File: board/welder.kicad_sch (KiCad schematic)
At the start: 48 parts, among them J1 VIN, J2 Conn_01x10, J3 Barrel_Jack_Switch, J4 USB_B, J5 POS, J6 NEG, J7 GND, Q1 Q_NIGBT_GCE, Q2 Q_NIGBT_GCE, Q3 Q_NIGBT_GCE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

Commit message: Add Cornell Dublier B10 footprint
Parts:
- C20: footprint (none) -> welder:Cornell_Dublier_B10
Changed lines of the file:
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@@
       (effects (font (size 1.27 1.27)) (justify left))
     )
-    (property "Footprint" "" (id 2) (at 379.4252 80.01 0)
+    (property "Footprint" "welder:Cornell_Dublier_B10" (id 2) (at 379.4252 80.01 0)
       (effects (font (size 1.27 1.27)) hide)
     )
@@
     )
     (path "/74e52290-b4a3-4f30-829f-bf68e89657d3"
-      (reference "C20") (unit 1) (value "50 uF") (footprint "")
+      (reference "C20") (unit 1) (value "50 uF") (footprint "welder:Cornell_Dublier_B10")
     )
     (path "/15aa1d89-1ae9-4558-9d8b-606633d6c749"

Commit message: Added big resistor and inductor footprints and updated board
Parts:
- FB1: footprint Inductor_SMD:L_0603_1608Metric -> Inductor_SMD:L_0805_2012Metric
- L1: footprint (none) -> welder:inductor
- R3: footprint (none) -> welder:RES_5931
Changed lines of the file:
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@@
     (property "Reference" "FB1" (id 0) (at 41.8592 118.11 90))
     (property "Value" "Ferrite_Bead" (id 1) (at 41.8592 120.65 90))
-    (property "Footprint" "Inductor_SMD:L_0603_1608Metric" (id 2) (at 41.91 123.952 90)
+    (property "Footprint" "Inductor_SMD:L_0805_2012Metric" (id 2) (at 41.91 123.952 90)
       (effects (font (size 1.27 1.27)) hide)
     )
@@
     (property "Reference" "R3" (id 0) (at 373.38 91.44 90))
     (property "Value" "0.0001" (id 1) (at 373.38 93.98 90))
-    (property "Footprint" "" (id 2) (at 373.38 102.108 90)
+    (property "Footprint" "welder:RES_5931" (id 2) (at 373.38 102.108 90)
       (effects (font (size 1.27 1.27)) hide)
     )
@@
     (property "Reference" "L1" (id 0) (at 373.38 45.72 90))
     (property "Value" "20 uH" (id 1) (at 373.38 48.26 90))
-    (property "Footprint" "" (id 2) (at 373.38 52.07 0)
+    (property "Footprint" "welder:inductor" (id 2) (at 373.38 52.07 0)
       (effects (font (size 1.27 1.27)) hide)
     )
@@
     )
     (path "/4385f506-0231-4a07-94dc-6e37a0993936"
-      (reference "FB1") (unit 1) (value "Ferrite_Bead") (footprint "Inductor_SMD:L_0603_1608Metric")
+      (reference "FB1") (unit 1) (value "Ferrite_Bead") (footprint "Inductor_SMD:L_0805_2012Metric")
     )
     (path "/9a2530d0-2be0-4564-82ea-55a5f02a536a"
@@
     )
     (path "/b52a224f-7f04-4e02-9abf-b091b5cdd9ca"
-      (reference "L1") (unit 1) (value "20 uH") (footprint "")
+      (reference "L1") (unit 1) (value "20 uH") (footprint "welder:inductor")
     )
     (path "/ba154238-685f-413a-8934-e53ce3e1c078"
@@
     )
     (path "/605c0c72-577a-420e-a1f2-9c549bf938f8"
-      (reference "R3") (unit 1) (value "0.0001") (footprint "")
+      (reference "R3") (unit 1) (value "0.0001") (footprint "welder:RES_5931")
     )
     (path "/070672ed-1ab6-4925-9102-8c9f7c67d003"

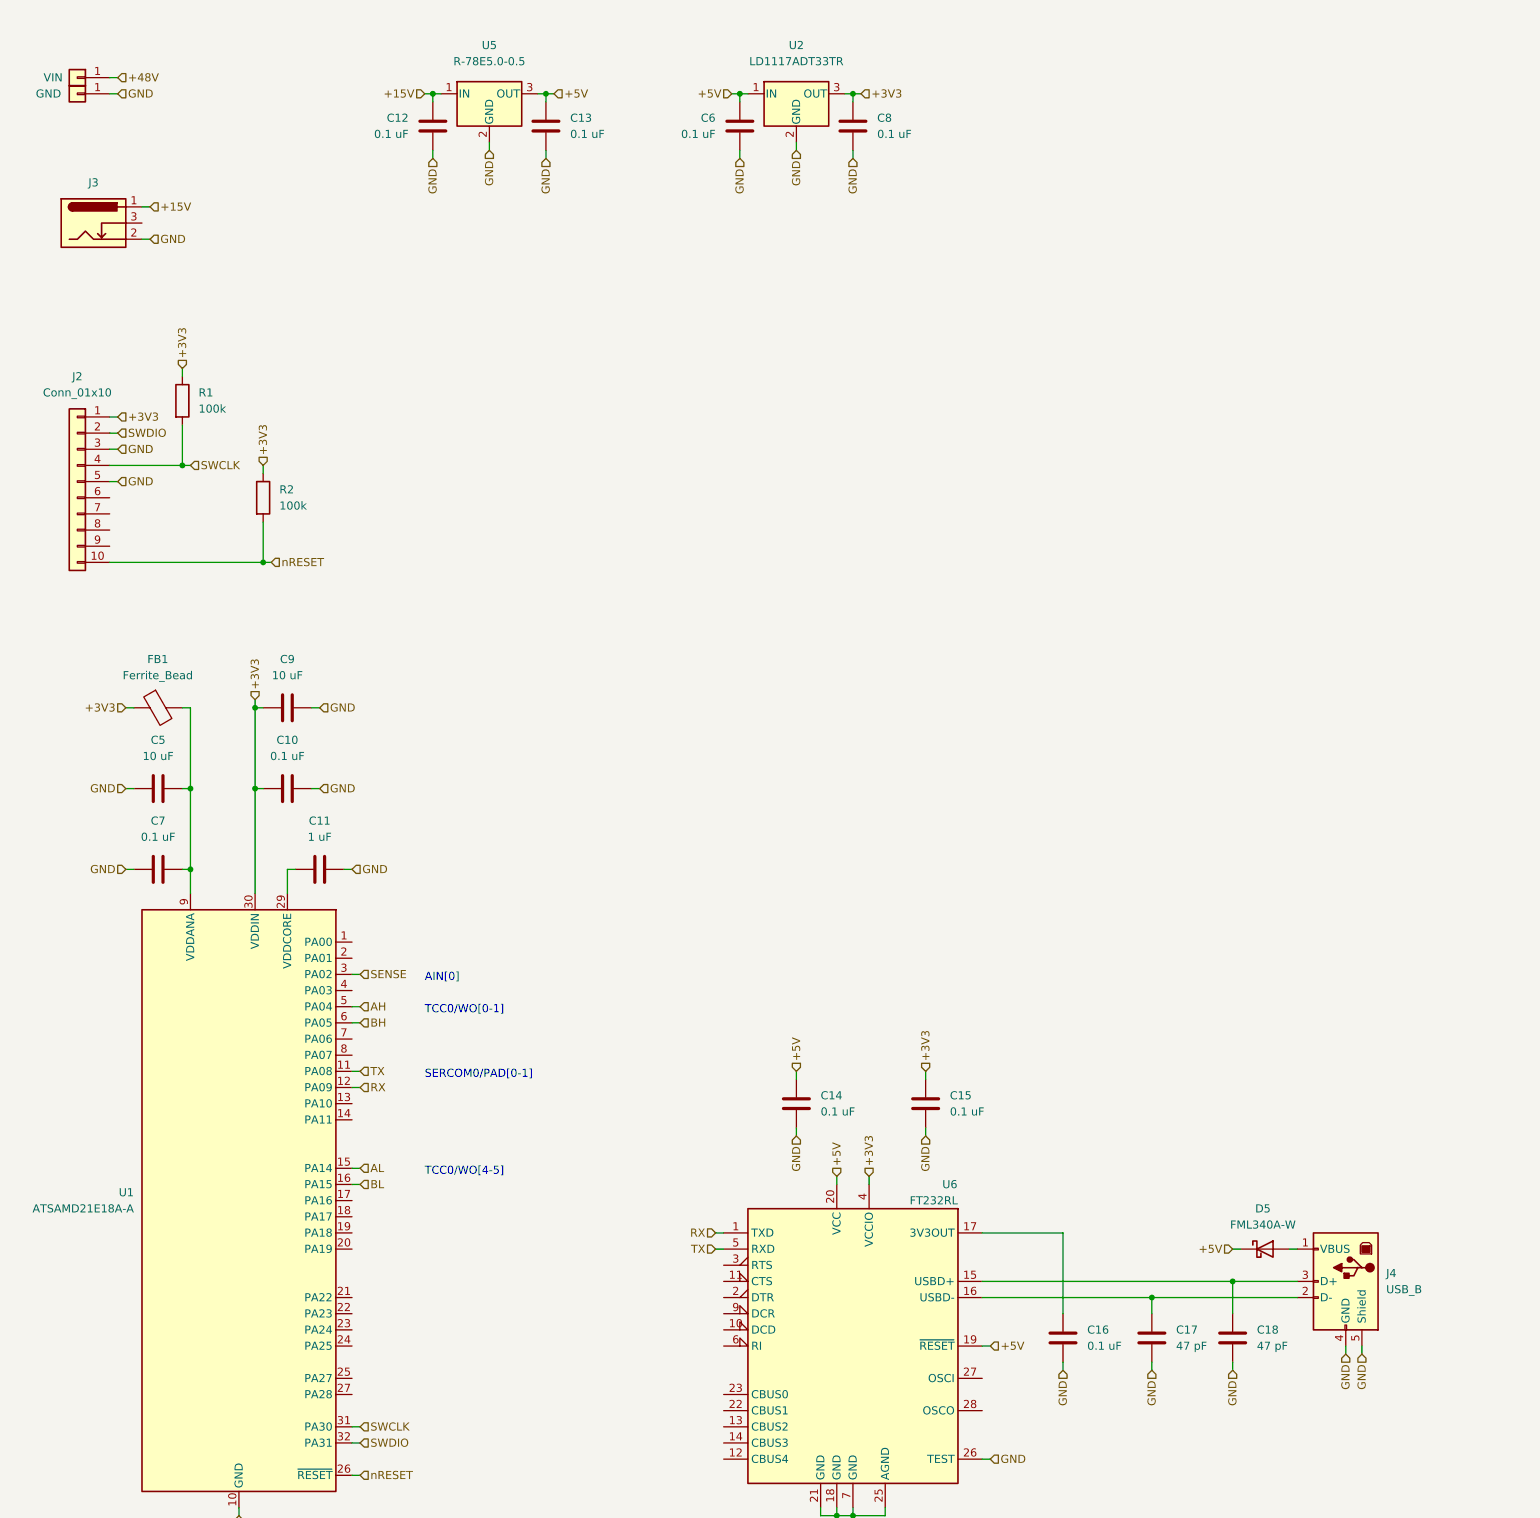
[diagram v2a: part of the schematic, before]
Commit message: added display, fixed up field names, updated board
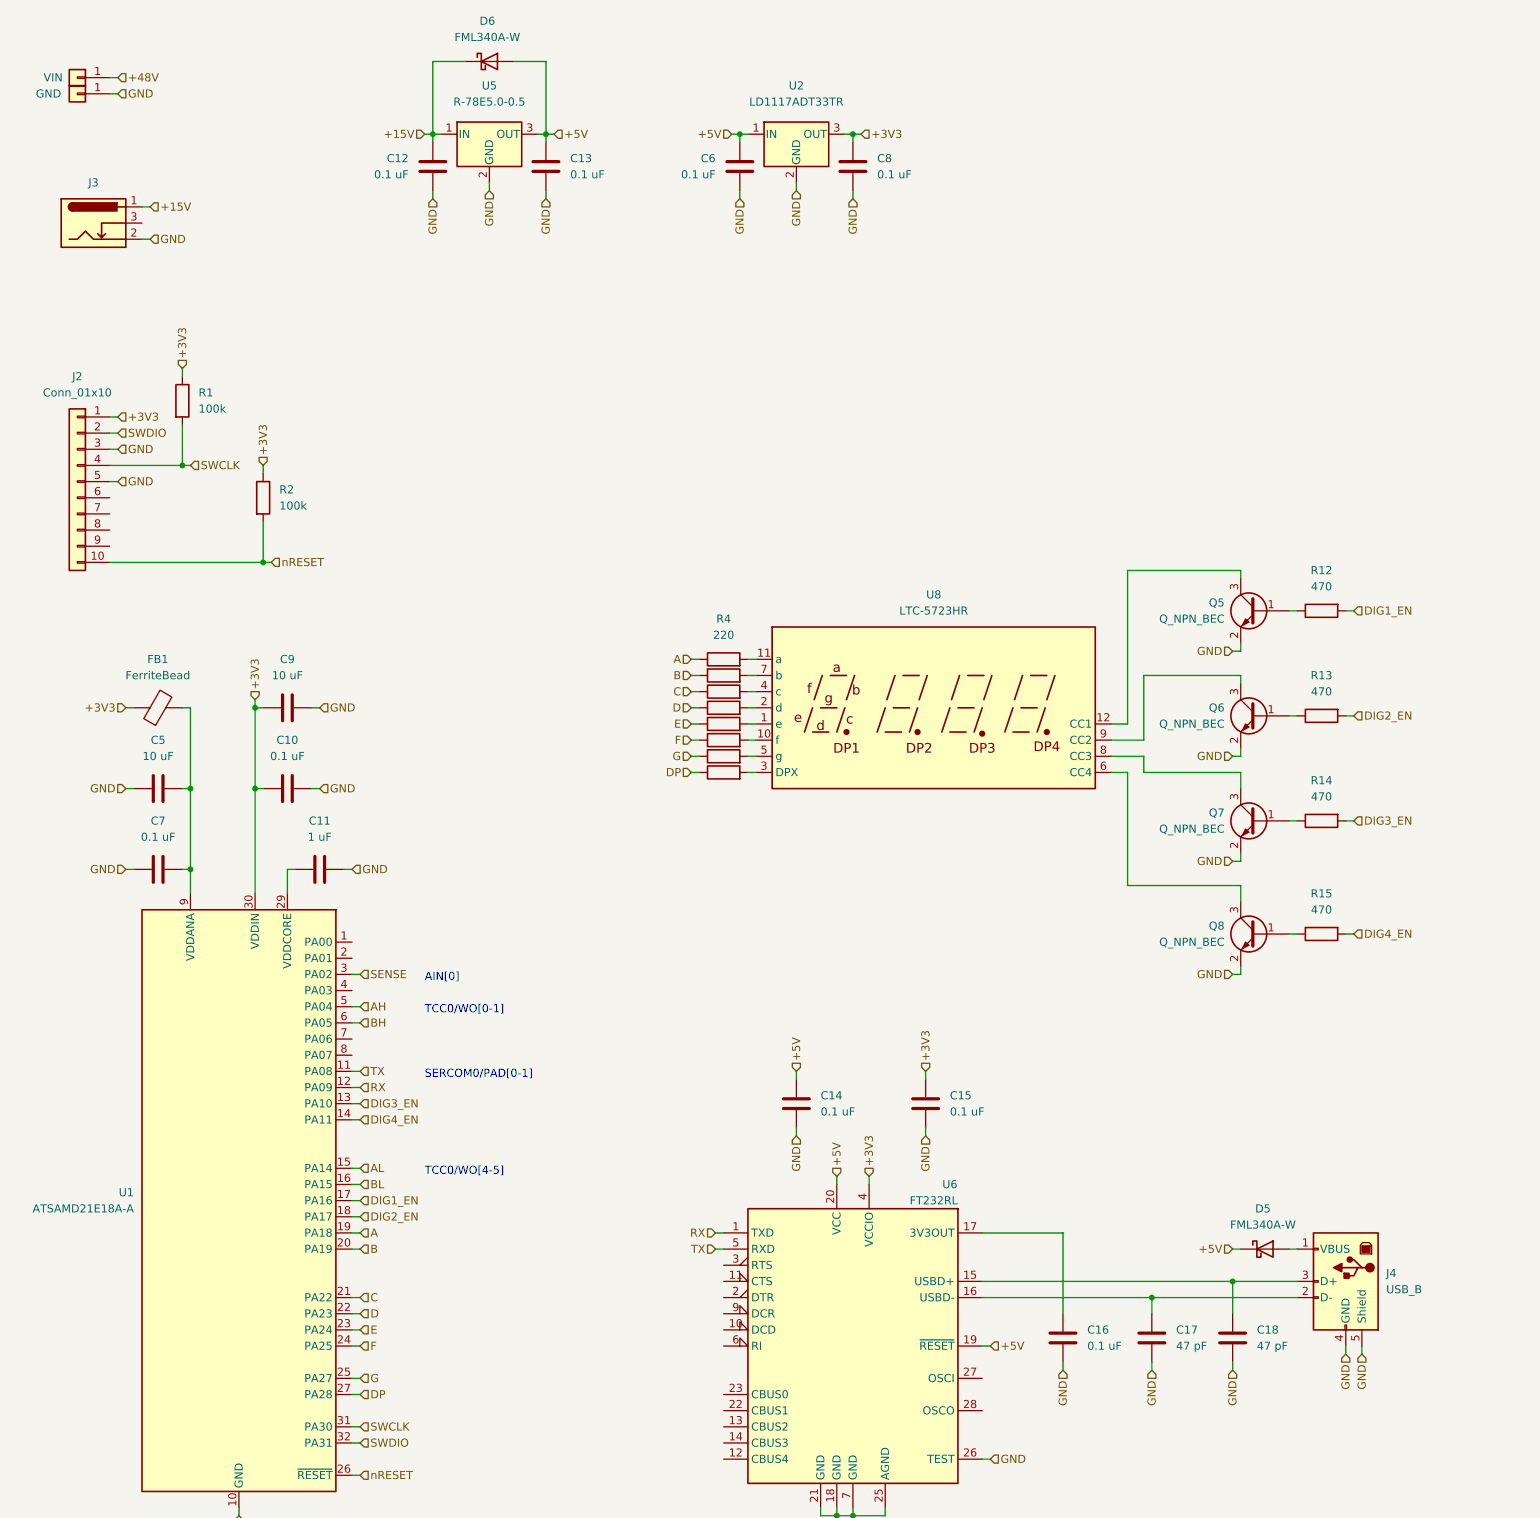
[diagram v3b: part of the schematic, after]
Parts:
- removed FB1: Ferrite_Bead, Inductor_SMD:L_0805_2012Metric, symbol cat-tracker-board-rescue:Ferrite_Bead-Device
- added D6: FML340A-W, Diode_SMD:D_SMA, symbol Device:D_Schottky
- added FB1: FerriteBead, Inductor_SMD:L_0805_2012Metric, symbol Device:FerriteBead
- added Q5, Q6, Q7, Q8: Q_NPN_BEC, Package_TO_SOT_SMD:SOT-23, symbol Device:Q_NPN_BEC
- added R10, R11, R4, R5, R6, R7, R8, R9: 220, Resistor_SMD:R_0805_2012Metric, symbol Device:R
- added R12, R13, R14, R15: 470, Resistor_SMD:R_0805_2012Metric, symbol Device:R
- added U8: LTC-5723HR, Display_7Segment:CA56-12EWA, symbol Display_Character:CC56-12EWA
- C1, C2, C3, C4: MFG1 Samsung Electro-Mechanics -> (none); MFG1PN CL32B475KCVZNWE -> (none); mfg1 (none) -> Samsung Electro-Mechanics; mfg1pn (none) -> CL32B475KCVZNWE
- C10, C12, C13, C14, C15, C16, C19, C6, C7, C8: MFG1 KEMET -> (none); MFG1PN C0805C104M5RACTU -> (none); mfg1 (none) -> KEMET; mfg1pn (none) -> C0805C104M5RACTU
- C11: footprint Capacitor_SMD:C_0603_1608Metric -> Capacitor_SMD:C_0805_2012Metric; MFG1 Samsung Electro-Mechanics -> (none); MFG1PN CL21B105KBFNFNE -> (none); mfg1 (none) -> Samsung Electro-Mechanics; mfg1pn (none) -> CL21B105KBFNFNE
- C17, C18: footprint Capacitor_SMD:C_0603_1608Metric -> Capacitor_SMD:C_0805_2012Metric; MFG1 KEMET -> (none); MFG1PN C0805C470J5GAC -> (none); mfg1 (none) -> KEMET; mfg1pn (none) -> C0805C470J5GAC
- C20: MFG1 Cornell Dubilier - CDE -> (none); MFG1PN BLH506K451B104 -> (none); mfg1 (none) -> Cornell Dubilier - CDE; mfg1pn (none) -> BLH506K451B104
- C5, C9: footprint Capacitor_SMD:C_0603_1608Metric -> Capacitor_SMD:C_0805_2012Metric; MFG1 Samsung Electro-Mechanics -> (none); MFG1PN CL32B106KBJNNNF -> (none); mfg1 (none) -> Samsung Electro-Mechanics; mfg1pn (none) -> CL32B106KBJNNNF
- D1, D2, D3, D4: MFG1 Rectron -> (none); MFG1PN 10A10-T -> (none); mfg1 (none) -> Rectron; mfg1pn (none) -> 10A10-T
- D5: MFG1 Rectron -> (none); MFG1PN FML340A-W -> (none); mfg1 (none) -> Rectron; mfg1pn (none) -> FML340A-W
- J1, J5, J6, J7, L1: exclude (none) -> yes
- J2: footprint Connector_PinHeader_1.27mm:PinHeader_2x05_P1.27mm_Horizontal -> Connector_PinHeader_1.27mm:PinHeader_2x05_P1.27mm_Vertical; MFG1 Samtec -> (none); MFG1PN FTSH-105-01-F-D-RA-K -> (none); mfg1 (none) -> Samtec; mfg1pn (none) -> FTSH-105-01-F-D-RA-K
- J3: MFG1 Kobiconn -> (none); MFG1PN 163-179PH-EX -> (none); mfg1 (none) -> Kobiconn; mfg1pn (none) -> 163-179PH-EX
- J4: MFG1 On Shore Technology Inc. -> (none); MFG1PN USB-B1HSB6 -> (none); mfg1 (none) -> On Shore Technology Inc.; mfg1pn (none) -> USB-B1HSB6
- Q1, Q2, Q3, Q4: MFG1 Microchip -> (none); MFG1PN APT95GR65B2 -> (none); mfg1 (none) -> Microchip; mfg1pn (none) -> APT95GR65B2
- R1, R2: footprint Resistor_SMD:R_0603_1608Metric -> Resistor_SMD:R_0805_2012Metric; MFG1 Panasonic -> (none); MFG1PN ERJ-3EKF1003V -> (none); mfg1 (none) -> Panasonic; mfg1pn (none) -> ERJ-3EKF1003V
- R3: MFG1 Vishay Dale -> (none); MFG1PN WSLP5931L1000FEA -> (none); mfg1 (none) -> Vishay Dale; mfg1pn (none) -> WSLP5931L1000FEA
- U1: MFG1 Microchip -> (none); MFG1PN ATSAMD21E18A-AU -> (none); mfg1 (none) -> Microchip; mfg1pn (none) -> ATSAMD21E18A-AU
- U2: MFG1 STMicroelectronics -> (none); MFG1PN LD1117ADT33TR -> (none); mfg1 (none) -> STMicroelectronics; mfg1pn (none) -> LD1117ADT33TR
- U3, U4: MFG1 Microchip -> (none); MFG1PN MIC4604YM -> (none); mfg1 (none) -> Microchip; mfg1pn (none) -> MIC4604YM
- U5: MFG1 Recom -> (none); MFG1PN R-78E5.0-0.5 -> (none); mfg1 (none) -> Recom; mfg1pn (none) -> R-78E5.0-0.5
- U6: MFG1 FTDI -> (none); MFG1PN FT232RL -> (none); mfg1 (none) -> FTDI; mfg1pn (none) -> FT232RL
- U7: MFG1 Texas Instruments -> (none); MFG1PN INA240A3D -> (none); MFG2 Texas Instruments -> (none); MFG2PN INA240A3DR -> (none); mfg1 (none) -> Texas Instruments; mfg1pn (none) -> INA240A3D; mfg2 (none) -> Texas Instruments; mfg2pn (none) -> INA240A3DR
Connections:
- net +15V: now also D6.1 (K)
- net +3V3: now also FB1.1
- net +5V: now also D6.2 (A)
- net GND: now also Q5.2 (E), Q6.2 (E), Q7.2 (E), Q8.2 (E)
- net DIG3_EN: now reaches U1.13 (PA10)
- net DIG3_EN: now also R14.2
- net DIG4_EN: now reaches U1.14 (PA11)
- net DIG4_EN: now also R15.2
- net DIG1_EN: now reaches U1.17 (PA16)
- net DIG1_EN: now also R12.2
- net DIG2_EN: now reaches U1.18 (PA17)
- net DIG2_EN: now also R13.2
- net A: now reaches U1.19 (PA18)
- net A: now also R4.1
- net B: now reaches U1.20 (PA19)
- net B: now also R5.1
- net C: now reaches U1.21 (PA22)
- net C: now also R6.1
- net D: now reaches U1.22 (PA23)
- net D: now also R7.1
- net E: now reaches U1.23 (PA24)
- net E: now also R8.1
- net F: now reaches U1.24 (PA25)
- net F: now also R9.1
- net G: now reaches U1.25 (PA27)
- net G: now also R10.1
- net DP: now reaches U1.27 (PA28)
- net DP: now also R11.1
- net at C5.1, C7.2, U1.9 (VDDANA): now also FB1.2
- new net: Q6.1 (B), R13.1
- new net: Q6.3 (C), U8.9 (CC2)
- new net: Q8.1 (B), R15.1
- new net: R9.2, U8.10 (f)
- new net: Q7.1 (B), R14.1
- new net: Q7.3 (C), U8.8 (CC3)
- new net: R7.2, U8.2 (d)
- new net: R11.2, U8.3 (DPX)
- new net: R4.2, U8.11 (a)
- new net: R10.2, U8.5 (g)
- new net: R8.2, U8.1 (e)
- new net: Q5.1 (B), R12.1
- new net: R5.2, U8.7 (b)
- new net: Q5.3 (C), U8.12 (CC1)
- new net: R6.2, U8.4 (c)
- new net: Q8.3 (C), U8.6 (CC4)
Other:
- moved on the sheet: C12, C13, C6, C8, U2, U5

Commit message: Add buttons, update board
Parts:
- added J8: EXT, TerminalBlock_Phoenix:TerminalBlock_Phoenix_MKDS-1,5-3_1x03_P5.00mm_Horizontal, symbol Connector_Generic:Conn_01x03
- added SW1: INC, Button_Switch_SMD:SW_SPST_PTS645, symbol Switch:SW_Push
- added SW2: DEC, Button_Switch_SMD:SW_SPST_PTS645, symbol Switch:SW_Push
- added SW3: SET, Button_Switch_SMD:SW_SPST_PTS645, symbol Switch:SW_Push
- added SW4: SEL, Button_Switch_SMD:SW_SPST_PTS645, symbol Switch:SW_Push
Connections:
- net +3V3: now also J8.1 (Pin_1)
- net GND: now also J8.3 (Pin_3), SW1.2, SW2.2, SW3.2, SW4.2
- net INC: now reaches U1.1 (PA00)
- net INC: now also SW1.1
- net DEC: now reaches U1.2 (PA01)
- net DEC: now also SW2.1
- net SET: now reaches U1.4 (PA03)
- net SET: now also SW3.1
- net SEL: now reaches U1.7 (PA06)
- net SEL: now also SW4.1
- net EXT: now reaches U1.8 (PA07)
- net EXT: now also J8.2 (Pin_2)
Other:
- moved on the sheet: Q5, Q6, Q7, Q8, R12, R13, R14, R15, R4, U8
